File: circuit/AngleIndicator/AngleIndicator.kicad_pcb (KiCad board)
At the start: 2 copper layers, 0 parts

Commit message: 回路図&PCB追加
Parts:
- added C1: 0.1u, Capacitor_SMD:C_0603_1608Metric_Pad1.08x0.95mm_HandSolder, F.Cu at (23.9, 47.8)
- added C2: 0.1u, Capacitor_SMD:C_0603_1608Metric_Pad1.08x0.95mm_HandSolder, F.Cu at (28.0, 60.7)
- added C3: 0.1u, Capacitor_SMD:C_0603_1608Metric_Pad1.08x0.95mm_HandSolder, F.Cu at (31.0, 53.3)
- added C4: 0.1u, Capacitor_SMD:C_0603_1608Metric_Pad1.08x0.95mm_HandSolder, F.Cu at (36.8, 50.1)
- added C5: 1.0u, Capacitor_SMD:C_0603_1608Metric_Pad1.08x0.95mm_HandSolder, F.Cu at (26.2, 54.9)
- added C6: 0.1u, Capacitor_SMD:C_0603_1608Metric_Pad1.08x0.95mm_HandSolder, F.Cu at (22.9, 44.5)
- added D1: LED, Diode_SMD:D_0603_1608Metric_Pad1.05x0.95mm_HandSolder, F.Cu at (39.0, 53.3)
- added G***: LOGO, AIOLIA:AIOLIA, F.Cu at (24.0, 29.2)
- added J1: Conn_01x06, Connector_JST:JST_ZH_B6B-ZR_1x06_P1.50mm_Vertical, F.Cu at (37.0, 47.1)
- added J2: Conn_01x04, Connector_JST:JST_PH_B4B-PH-SM4-TB_1x04-1MP_P2.00mm_Vertical, F.Cu at (30.1, 65.2)
- added R2: 100, Resistor_SMD:R_0603_1608Metric_Pad0.98x0.95mm_HandSolder, F.Cu at (39.0, 56.7)
- added R3: 100, Resistor_SMD:R_0603_1608Metric_Pad0.98x0.95mm_HandSolder, F.Cu at (27.0, 39.7)
- added R4: 100, Resistor_SMD:R_0603_1608Metric_Pad0.98x0.95mm_HandSolder, F.Cu at (27.0, 41.2)
- added R5: 120, Resistor_SMD:R_0603_1608Metric_Pad0.98x0.95mm_HandSolder, F.Cu at (32.1, 60.7)
- added U1: ~, AIOLIA:SOT95P280X130-5N, F.Cu at (27.9, 57.7)
- added U2: STM32G441KBTx, Package_QFP:LQFP-32_7x7mm_P0.8mm, F.Cu at (29.9, 47.3)
- added U3: ~, Package_TO_SOT_SMD:SOT-23-8_Handsoldering, F.Cu at (32.1, 57.4)
- added U4: ~, Package_SO:SOIC-8_3.9x4.9mm_P1.27mm, F.Cu at (30.0, 30.0)
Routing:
- net +3V3: track 0.00 -> 74.4 mm, vias 0 -> 1
- net RX2: track 0.00 -> 13.2 mm, vias 0 -> 1
- net TX2: track 0.00 -> 12.8 mm, vias 0 -> 1
- net GND: track 0.00 -> 12.6 mm, vias 0 -> 86
- net CAN_TX: track 0.00 -> 12.0 mm, vias 0 -> 2
- net SCL: track 0.00 -> 11.5 mm
- net CAN_RX: track 0.00 -> 11.0 mm, vias 0 -> 2
- net SDA: track 0.00 -> 10.9 mm
- net VCC: track 0.00 -> 8.92 mm
- net LED1: track 0.00 -> 8.44 mm
- net /CAN-: track 0.00 -> 6.34 mm
- net /CAN+: track 0.00 -> 6.32 mm
- net SWCLK: track 0.00 -> 4.25 mm
- net SWDIO: track 0.00 -> 3.45 mm
- net /BOOT0: track 0.00 -> 3.44 mm
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- added copper zone on B.Cu, net GND
- added copper zone on F.Cu, net GND
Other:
- board outline added: 20 x 50 mm
- board text added: "3v3"
- board text added: "GND"
- board text added: "RXD"
- board text added: "SWCLK"
- board text added: "SWDIO"
- board text added: "TXD"

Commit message: 1/09発注分
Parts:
- G***, J1: moved to B.Cu
- J2: footprint Connector_JST:JST_PH_B4B-PH-SM4-TB_1x04-1MP_P2.00mm_Vertical -> Connector_JST:JST_PH_S4B-PH-K_1x04_P2.00mm_Horizontal; moved to B.Cu
- moved G*** 25.5 mm to (37.0, 51.1), turned to 180 degrees
- moved J2 3.60 mm to (33.0, 63.1)
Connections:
- U2 pad 26: unconnected-(U2-PB3-Pad26) -> DIR
- U4 pad 8: unconnected-(U4-DIR-Pad8) -> DIR
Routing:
- net DIR: track 0.00 -> 10.6 mm, vias 0 -> 2
- net /CAN+: track 6.32 -> 4.64 mm
- net GND: track 12.6 -> 10.9 mm, vias 86 -> 85
- net VCC: track 8.92 -> 7.32 mm
- net /CAN-: track 6.34 -> 4.74 mm
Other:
- board text added: "Angle Indicator"
- board text added: "CANH"
- board text added: "CANL"
- board text added: "J2"
- board text added: "VCC"
- board text added: "designed by xsuz"

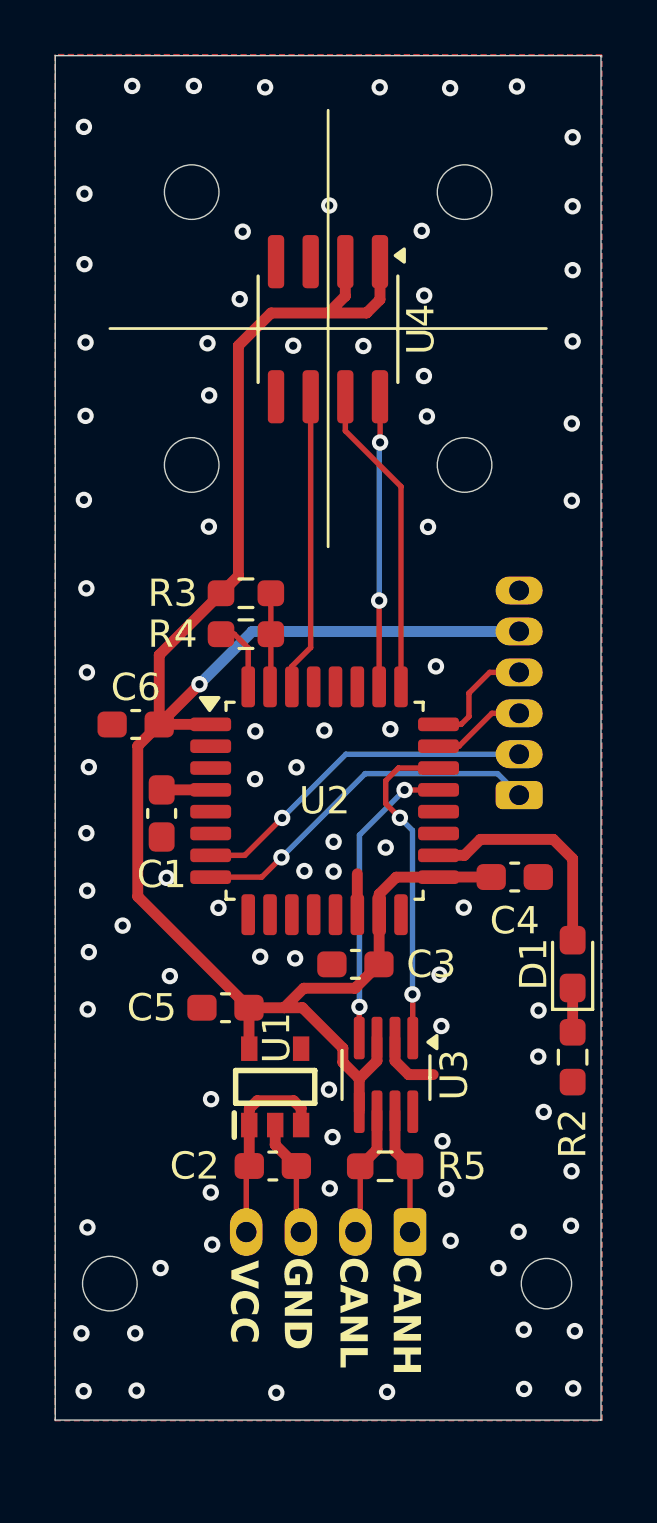
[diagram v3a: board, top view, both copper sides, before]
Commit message: pull-up抵抗とアナログ入力を追加
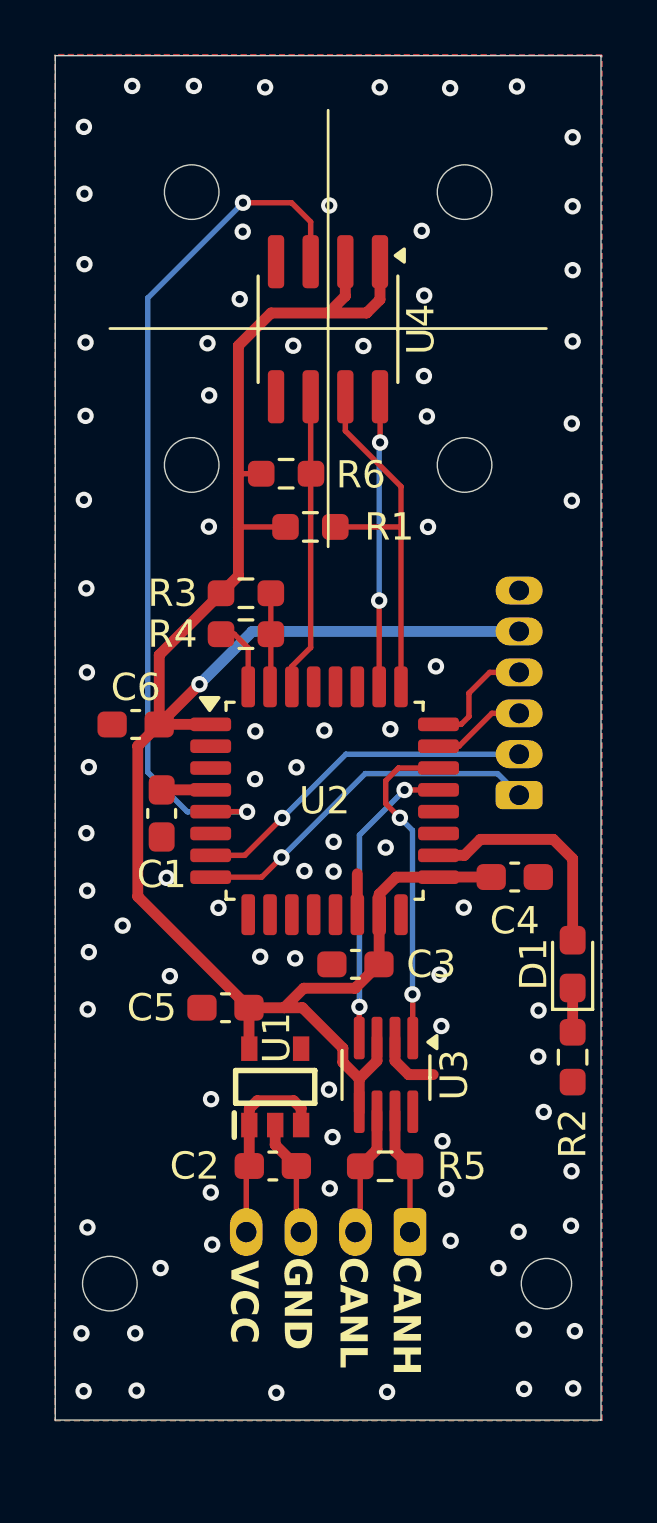
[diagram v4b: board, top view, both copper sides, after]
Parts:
- added R1: 10k, Resistor_SMD:R_0603_1608Metric_Pad0.98x0.95mm_HandSolder, F.Cu at (29.4, 37.3)
- added R6: 10k, Resistor_SMD:R_0603_1608Metric_Pad0.98x0.95mm_HandSolder, F.Cu at (28.5, 35.3)
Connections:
- U2 pad 5: unconnected-(U2-PA0-Pad5) -> AIN
- U4 pad 3: unconnected-(U4-OUT-Pad3) -> AIN
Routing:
- net AIN: track 0.00 -> 32.1 mm, vias 0 -> 2
- net +3V3: track 74.4 -> 77.0 mm
- net SCL: track 11.5 -> 13.9 mm

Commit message: シルクを更新
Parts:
- moved G*** 1.00 mm to (36.6, 50.2), turned to -150 degrees
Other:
- board text added: "rev 2. - added pull-up register - added analog input"

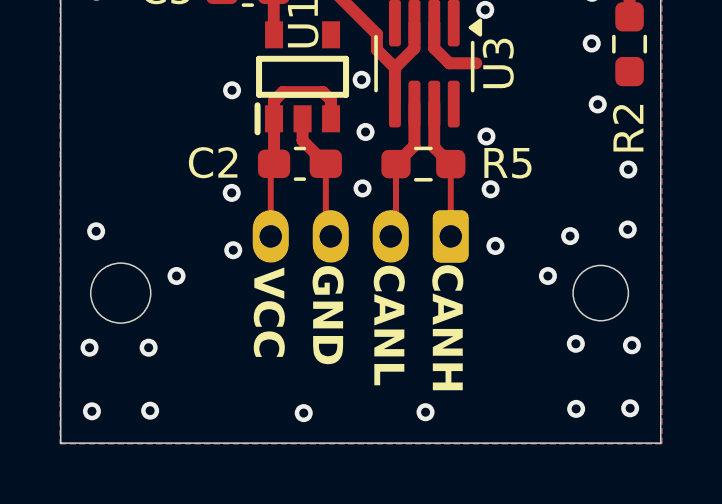
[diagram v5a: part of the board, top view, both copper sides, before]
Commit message: CANコネクタの配置を変更
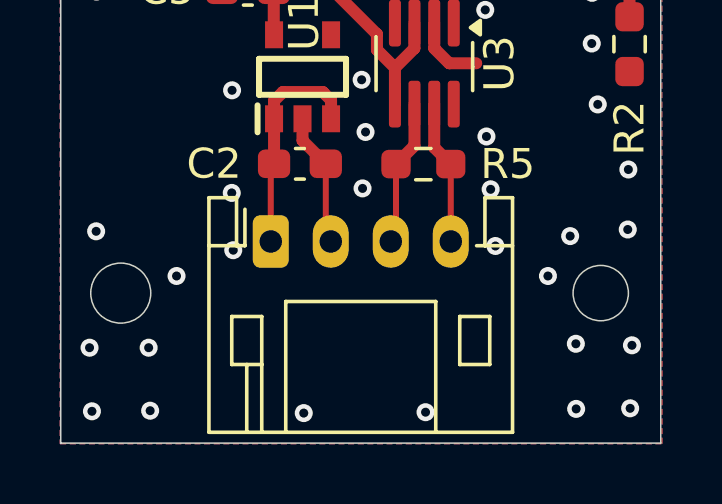
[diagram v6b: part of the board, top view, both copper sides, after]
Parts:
- J2: moved to F.Cu
- moved J2 6.00 mm to (27.0, 63.3), turned to 0 degrees
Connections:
- J2 pad 1: /CAN+ -> VCC
- J2 pad 2: /CAN- -> GND
- J2 pad 3: GND -> /CAN-
- J2 pad 4: VCC -> /CAN+
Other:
- board text removed: "J2"
